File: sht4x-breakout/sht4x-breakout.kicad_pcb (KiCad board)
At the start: 2 copper layers, 19 x 19 mm, 5 parts, among them U1 SHT4x

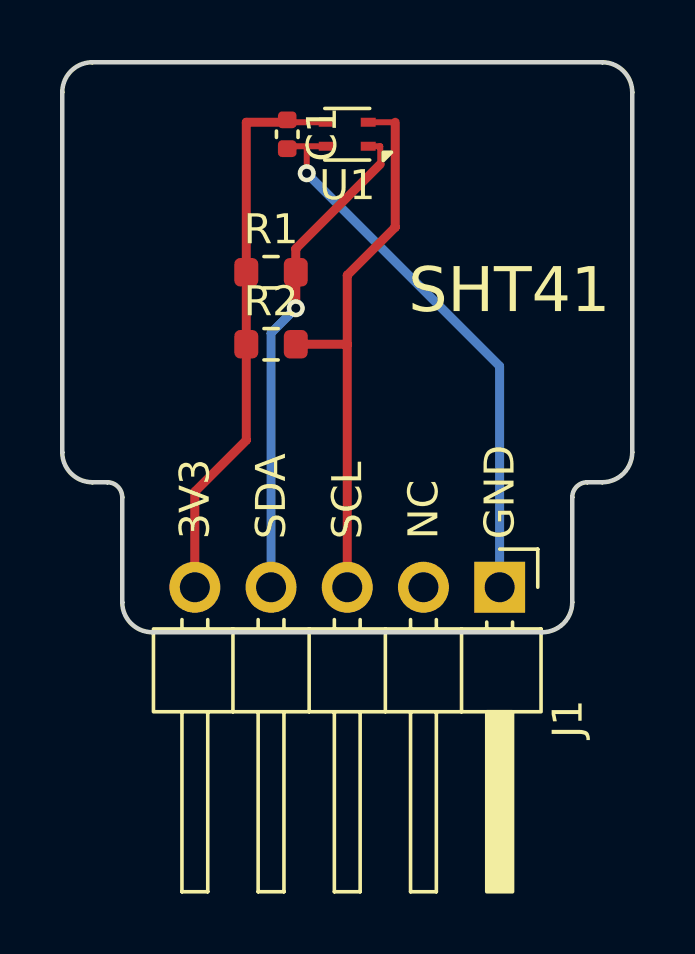
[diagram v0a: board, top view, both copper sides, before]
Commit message: Breakout board revision 2: square outline and mounting hole - Changed the outline to a plain 19 x 19 mm square, removing the narrow header end - Added an M2.5 mounting hole (H1) at X 2.7, Y 2.7 to the schematic and PCB - J1 uses the vertical header footprint for cleaner silkscreen, with the right-angle 3D model - Set the board design rules to JLCPCB's manufacturing limits - Hid the PWR_FLAG values in the schematic
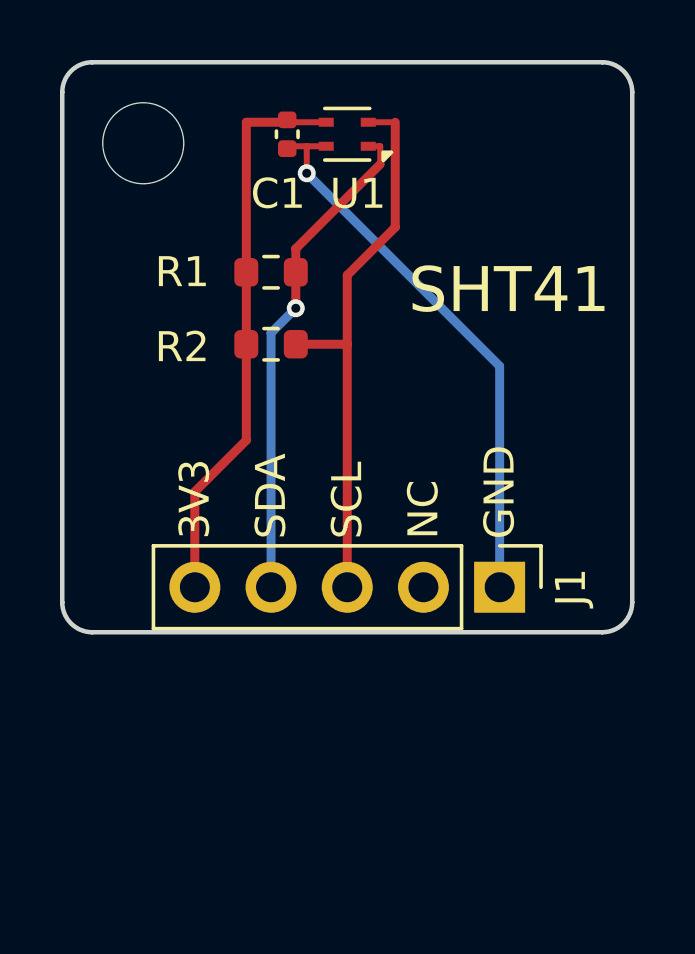
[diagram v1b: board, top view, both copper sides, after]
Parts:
- added H1: MountingHole, MountingHole:MountingHole_2.7mm_M2.5, F.Cu at (102.7, 102.7)
- J1: footprint Connector_PinHeader_2.54mm:PinHeader_1x05_P2.54mm_Horizontal -> Connector_PinHeader_2.54mm:PinHeader_1x05_P2.54mm_Vertical
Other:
- outline, holes or cut-outs redrawn
- rule solder_mask_min_width: 0.25 -> 0.1
- board text added: "REV ${REVISION}"
- board text removed: "REV 1"

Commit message: Minor adjustments and label changes
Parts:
- J1: value ~ -> 1x5 R/A header
- U1: value SHT4x -> SHT41-AD1B-R2
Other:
- board text added: "AL141"
- board text removed: "I2C 0x44"
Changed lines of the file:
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@@
 			)
 		)
-		(property "Value" "SHT4x"
+		(property "Value" "SHT41-AD1B-R2"
 			(at 0 1.7 180)
 			(layer "F.Fab")
@@
 			)
 		)
-		(property "Value" "~"
+		(property "Value" "1x5 R/A header"
 			(at 0 12.54 90)
 			(layer "F.Fab")
@@
 		(fp_line
 			(start -1.38 11.54)
-			(end 1.38 11.54)
+			(end 1.2 11.54)
 			(stroke
 				(width 0.12)
@@
 		(fp_line
 			(start -1.38 1.27)
-			(end 1.38 1.27)
-			(stroke
-				(width 0.12)
-				(type solid)
-			)
-			(layer "F.SilkS")
-		)
-		(fp_line
-			(start 1.38 1.27)
-			(end 1.38 11.54)
+			(end 1.2 1.27)
+			(stroke
+				(width 0.12)
+				(type solid)
+			)
+			(layer "F.SilkS")
+		)
+		(fp_line
+			(start 1.2 1.27)
+			(end 1.2 11.54)
 			(stroke
 				(width 0.12)
@@
 		)
 	)
-	(gr_text "I2C 0x44"
+	(gr_text "AL141"
 		(at 109.5 107 0)
 		(layer "B.SilkS")

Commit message: Silkscreen adjustments, added OSHW logos
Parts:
- added REF**: OSHW-Symbol_6.7x6mm_SilkScreen, Symbol:OSHW-Symbol_6.7x6mm_SilkScreen, B.Cu at (114.7, 103.6)
